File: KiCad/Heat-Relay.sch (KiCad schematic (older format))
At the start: 6 parts

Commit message: controller board schematic complete
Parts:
- gave numbers to parts that had none: 6
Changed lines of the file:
@@
 $Descr A4 11693 8268
 encoding utf-8
-Sheet 3 5
+Sheet 3 6
 Title ""
 Date ""
@@
 Heat
 $Comp
-L G5LE-1A-E_DC12 K?
+L G5LE-1A-E_DC12 K1
 U 1 1 568008CE
 P 7100 3250
-F 0 "K?" H 7850 3350 50  0000 L CNN
+F 0 "K1" H 7850 3350 50  0000 L CNN
 F 1 "G5LE-1A-E_DC12" H 7850 3200 50  0000 L CNN
 F 2 "" H 7100 3250 50  0000 C CNN
@@
 $EndComp
 $Comp
-L MJE340 Q?
+L MJE340 Q2
 U 1 1 5680095F
 P 6300 4400
-F 0 "Q?" H 6500 4475 50  0000 L CNN
+F 0 "Q2" H 6500 4475 50  0000 L CNN
 F 1 "MJE340" H 6500 4400 50  0000 L CNN
 F 2 "TO-126" H 6500 4325 50  0000 L CIN
@@
 $EndComp
 $Comp
-L D D?
+L D D1
 U 1 1 56800A86
 P 6400 3250
-F 0 "D?" V 6300 3100 50  0000 R CNN
+F 0 "D1" V 6300 3100 50  0000 R CNN
 F 1 "V*A(max) > 0.4 W" V 6450 3100 50  0000 R CNN
 F 2 "" H 6400 3250 50  0000 C CNN
@@
 HeatLive
 $Comp
-L VAA #PWR?
+L VAA #PWR28
 U 1 1 56800D0A
 P 7650 2200
-F 0 "#PWR?" H 7650 2050 50  0001 C CNN
+F 0 "#PWR28" H 7650 2050 50  0001 C CNN
 F 1 "VAA" H 7650 2350 50  0000 C CNN
 F 2 "" H 7650 2200 50  0000 C CNN
@@
 $EndComp
 $Comp
-L +12V #PWR?
+L +12V #PWR26
 U 1 1 56800DC1
 P 6400 2200
-F 0 "#PWR?" H 6400 2050 50  0001 C CNN
+F 0 "#PWR26" H 6400 2050 50  0001 C CNN
 F 1 "+12V" H 6400 2340 50  0000 C CNN
 F 2 "" H 6400 2200 50  0000 C CNN
@@
 DoorC2
 $Comp
-L R R?
+L R R23
 U 1 1 56800FE2
 P 5500 4950
-F 0 "R?" V 5580 4950 50  0000 C CNN
+F 0 "R23" V 5580 4950 50  0000 C CNN
 F 1 "333" V 5500 4950 50  0000 C CNN
 F 2 "" V 5430 4950 50  0000 C CNN
@@
 $EndComp
 $Comp
-L R R?
+L R R22
 U 1 1 5680103F
 P 3550 4400
-F 0 "R?" V 3630 4400 50  0000 C CNN
+F 0 "R22" V 3630 4400 50  0000 C CNN
 F 1 "1k" V 3550 4400 50  0000 C CNN
 F 2 "" V 3480 4400 50  0000 C CNN
@@
 $EndComp
 $Comp
-L R R?
+L R R21
 U 1 1 5680107F
 P 3000 3950
-F 0 "R?" V 3080 3950 50  0000 C CNN
+F 0 "R21" V 3080 3950 50  0000 C CNN
 F 1 "10k" V 3000 3950 50  0000 C CNN
 F 2 "" V 2930 3950 50  0000 C CNN
@@
 $EndComp
 $Comp
-L VDD #PWR?
+L VDD #PWR24
 U 1 1 56801231
 P 3000 3300
-F 0 "#PWR?" H 3000 3150 50  0001 C CNN
+F 0 "#PWR24" H 3000 3150 50  0001 C CNN
 F 1 "VDD" H 3000 3450 50  0000 C CNN
 F 2 "" H 3000 3300 50  0000 C CNN
@@
 Connection ~ 5500 4400
 $Comp
-L GND #PWR?
+L GND #PWR25
 U 1 1 56801366
 P 5500 5400
-F 0 "#PWR?" H 5500 5150 50  0001 C CNN
+F 0 "#PWR25" H 5500 5150 50  0001 C CNN
 F 1 "GND" H 5500 5250 50  0000 C CNN
 F 2 "" H 5500 5400 50  0000 C CNN
@@
 $EndComp
 $Comp
-L GND #PWR?
+L GND #PWR27
 U 1 1 56801386
 P 6400 5400
-F 0 "#PWR?" H 6400 5150 50  0001 C CNN
+F 0 "#PWR27" H 6400 5150 50  0001 C CNN
 F 1 "GND" H 6400 5250 50  0000 C CNN
 F 2 "" H 6400 5400 50  0000 C CNN

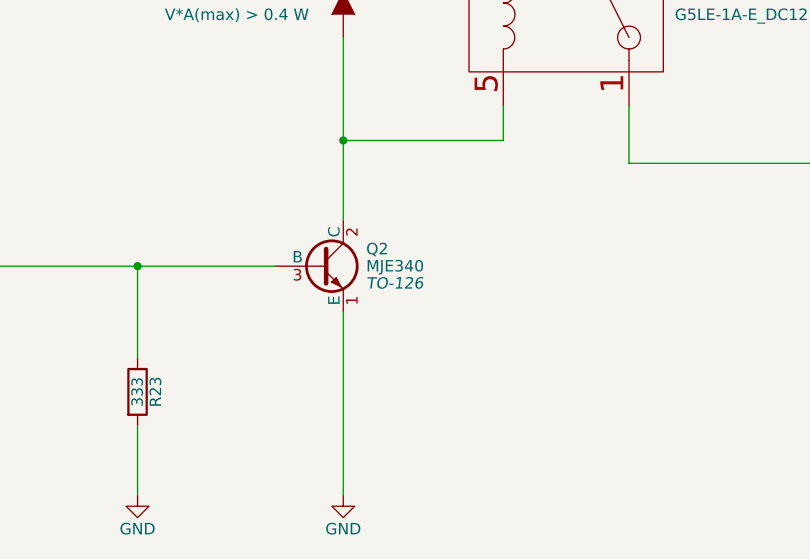
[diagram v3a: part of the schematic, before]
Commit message: HeatOn fix, replaced R1-8 with array
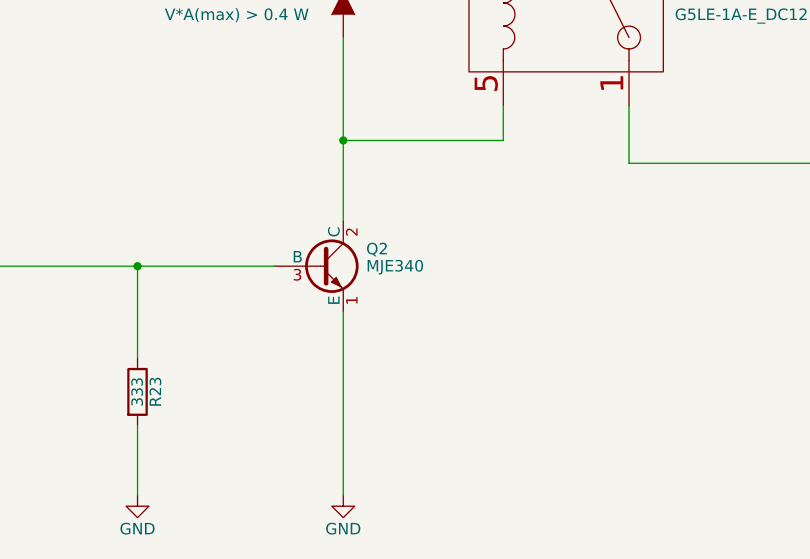
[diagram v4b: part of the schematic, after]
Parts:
- Q2: footprint TO-126 -> (none)
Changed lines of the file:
@@
 F 0 "K1" H 7850 3350 50  0000 L CNN
 F 1 "G5LE-1A-E_DC12" H 7850 3200 50  0000 L CNN
-F 2 "" H 7100 3250 50  0000 C CNN
+F 2 "" H 7100 3250 50  0001 C CNN
 F 3 "" H 7100 3250 50  0000 C CNN
 	1    7100 3250
@@
 F 0 "Q2" H 6500 4475 50  0000 L CNN
 F 1 "MJE340" H 6500 4400 50  0000 L CNN
-F 2 "TO-126" H 6500 4325 50  0000 L CIN
+F 2 "" H 6500 4325 50  0001 L CIN
 F 3 "" H 6300 4400 50  0000 L CNN
 	1    6300 4400
@@
 F 0 "D1" V 6300 3100 50  0000 R CNN
 F 1 "V*A(max) > 0.4 W" V 6450 3100 50  0000 R CNN
-F 2 "" H 6400 3250 50  0000 C CNN
+F 2 "" H 6400 3250 50  0001 C CNN
 F 3 "" H 6400 3250 50  0000 C CNN
 	1    6400 3250
@@
 HeatLive
 $Comp
-L VAA #PWR28
+L VAA #PWR024
 U 1 1 56800D0A
 P 7650 2200
-F 0 "#PWR28" H 7650 2050 50  0001 C CNN
+F 0 "#PWR024" H 7650 2050 50  0001 C CNN
 F 1 "VAA" H 7650 2350 50  0000 C CNN
 F 2 "" H 7650 2200 50  0000 C CNN
@@
 $EndComp
 $Comp
-L +12V #PWR26
+L +12V #PWR025
 U 1 1 56800DC1
 P 6400 2200
-F 0 "#PWR26" H 6400 2050 50  0001 C CNN
+F 0 "#PWR025" H 6400 2050 50  0001 C CNN
 F 1 "+12V" H 6400 2340 50  0000 C CNN
 F 2 "" H 6400 2200 50  0000 C CNN
@@
 F 0 "R23" V 5580 4950 50  0000 C CNN
 F 1 "333" V 5500 4950 50  0000 C CNN
-F 2 "" V 5430 4950 50  0000 C CNN
+F 2 "" V 5430 4950 50  0001 C CNN
 F 3 "" H 5500 4950 50  0000 C CNN
 	1    5500 4950
@@
 F 0 "R22" V 3630 4400 50  0000 C CNN
 F 1 "1k" V 3550 4400 50  0000 C CNN
-F 2 "" V 3480 4400 50  0000 C CNN
+F 2 "" V 3480 4400 50  0001 C CNN
 F 3 "" H 3550 4400 50  0000 C CNN
 	1    3550 4400
@@
 F 0 "R21" V 3080 3950 50  0000 C CNN
 F 1 "10k" V 3000 3950 50  0000 C CNN
-F 2 "" V 2930 3950 50  0000 C CNN
+F 2 "" V 2930 3950 50  0001 C CNN
 F 3 "" H 3000 3950 50  0000 C CNN
 	1    3000 3950
@@
 $EndComp
 $Comp
-L VDD #PWR24
+L VDD #PWR026
 U 1 1 56801231
 P 3000 3300
-F 0 "#PWR24" H 3000 3150 50  0001 C CNN
+F 0 "#PWR026" H 3000 3150 50  0001 C CNN
 F 1 "VDD" H 3000 3450 50  0000 C CNN
 F 2 "" H 3000 3300 50  0000 C CNN
@@
 Connection ~ 5500 4400
 $Comp
-L GND #PWR25
+L GND #PWR027
 U 1 1 56801366
 P 5500 5400
-F 0 "#PWR25" H 5500 5150 50  0001 C CNN
+F 0 "#PWR027" H 5500 5150 50  0001 C CNN
 F 1 "GND" H 5500 5250 50  0000 C CNN
 F 2 "" H 5500 5400 50  0000 C CNN
@@
 $EndComp
 $Comp
-L GND #PWR27
+L GND #PWR028
 U 1 1 56801386
 P 6400 5400
-F 0 "#PWR27" H 6400 5150 50  0001 C CNN
+F 0 "#PWR028" H 6400 5150 50  0001 C CNN
 F 1 "GND" H 6400 5250 50  0000 C CNN
 F 2 "" H 6400 5400 50  0000 C CNN

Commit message: kicad resistor package associations complete
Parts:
- R21, R22, R23: footprint (none) -> Resistors_ThroughHole:Resistor_Horizontal_RM10mm
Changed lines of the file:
@@
 F 0 "R23" V 5580 4950 50  0000 C CNN
 F 1 "333" V 5500 4950 50  0000 C CNN
-F 2 "" V 5430 4950 50  0001 C CNN
+F 2 "Resistors_ThroughHole:Resistor_Horizontal_RM10mm" V 5430 4950 50  0001 C CNN
 F 3 "" H 5500 4950 50  0000 C CNN
 	1    5500 4950
@@
 F 0 "R22" V 3630 4400 50  0000 C CNN
 F 1 "1k" V 3550 4400 50  0000 C CNN
-F 2 "" V 3480 4400 50  0001 C CNN
+F 2 "Resistors_ThroughHole:Resistor_Horizontal_RM10mm" V 3480 4400 50  0001 C CNN
 F 3 "" H 3550 4400 50  0000 C CNN
 	1    3550 4400
@@
 F 0 "R21" V 3080 3950 50  0000 C CNN
 F 1 "10k" V 3000 3950 50  0000 C CNN
-F 2 "" V 2930 3950 50  0001 C CNN
+F 2 "Resistors_ThroughHole:Resistor_Horizontal_RM10mm" V 2930 3950 50  0001 C CNN
 F 3 "" H 3000 3950 50  0000 C CNN
 	1    3000 3950

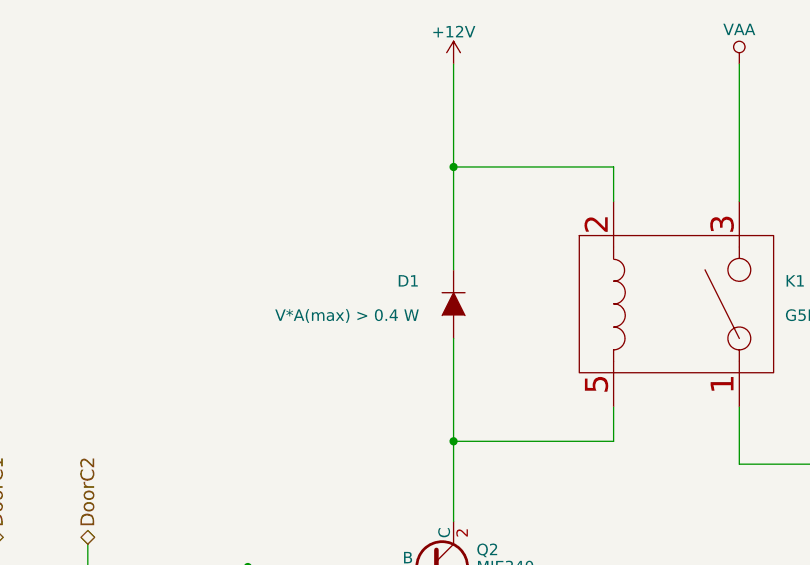
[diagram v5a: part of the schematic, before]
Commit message: capacitors and diode part associations
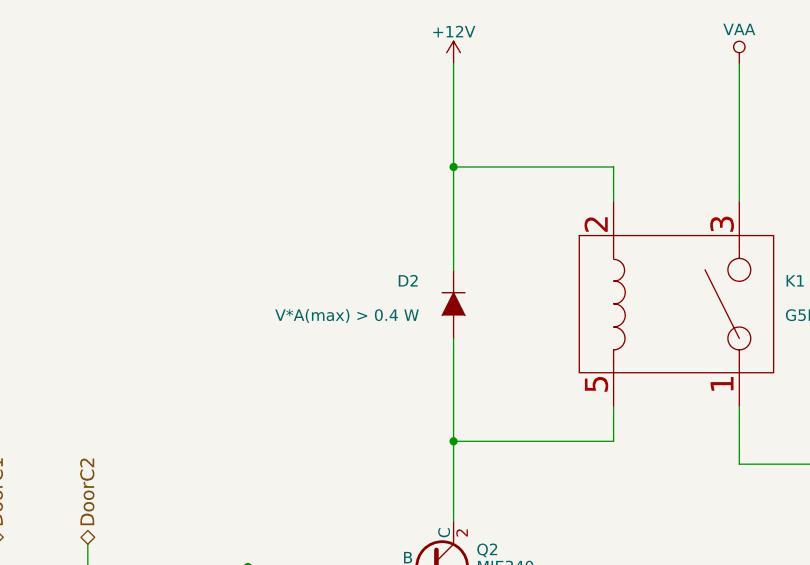
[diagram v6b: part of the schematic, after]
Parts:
- D2: renamed from D1; footprint (none) -> Discret:D3
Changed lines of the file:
@@
 $EndComp
 $Comp
-L D D1
+L D D2
 U 1 1 56800A86
 P 6400 3250
-F 0 "D1" V 6300 3100 50  0000 R CNN
+F 0 "D2" V 6300 3100 50  0000 R CNN
 F 1 "V*A(max) > 0.4 W" V 6450 3100 50  0000 R CNN
-F 2 "" H 6400 3250 50  0001 C CNN
+F 2 "Discret:D3" H 6400 3250 50  0001 C CNN
 F 3 "" H 6400 3250 50  0000 C CNN
 	1    6400 3250

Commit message: footprint associations complete
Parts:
- K1: footprint (none) -> Easy-PCB-footprints:G5LE-1A-E_DC12
- Q2: footprint (none) -> Easy-PCB-footprints:MJE3x0
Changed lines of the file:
@@
 F 0 "K1" H 7850 3350 50  0000 L CNN
 F 1 "G5LE-1A-E_DC12" H 7850 3200 50  0000 L CNN
-F 2 "" H 7100 3250 50  0001 C CNN
+F 2 "Easy-PCB-footprints:G5LE-1A-E_DC12" H 7100 3250 50  0001 C CNN
 F 3 "" H 7100 3250 50  0000 C CNN
 	1    7100 3250
@@
 F 0 "Q2" H 6500 4475 50  0000 L CNN
 F 1 "MJE340" H 6500 4400 50  0000 L CNN
-F 2 "" H 6500 4325 50  0001 L CIN
+F 2 "Easy-PCB-footprints:MJE3x0" H 6500 4325 50  0001 L CIN
 F 3 "" H 6300 4400 50  0000 L CNN
 	1    6300 4400

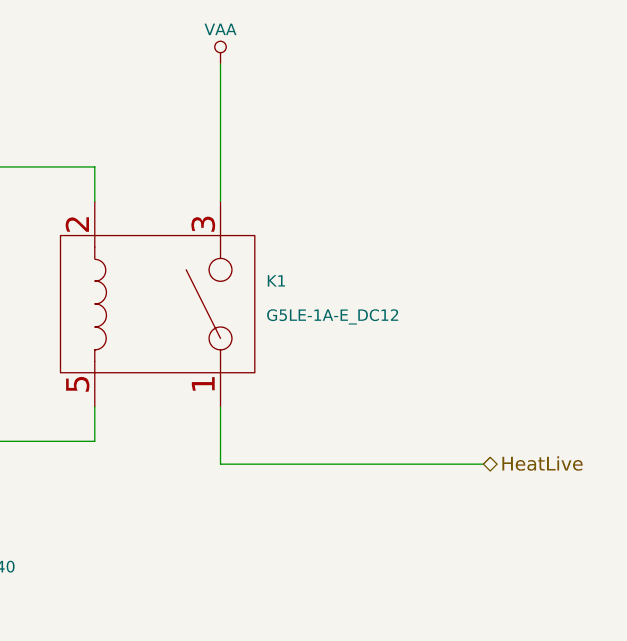
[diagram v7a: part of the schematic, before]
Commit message: power port, switch, transformer, and relay in place
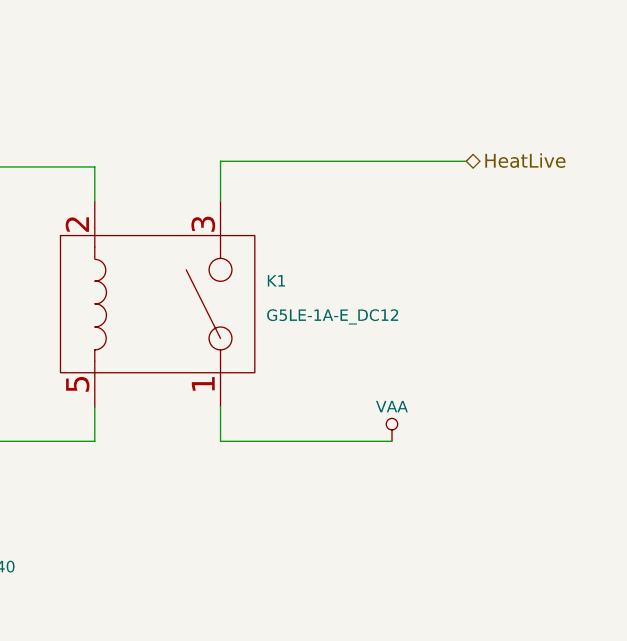
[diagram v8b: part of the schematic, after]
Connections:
- net HeatLive: now also K1.3 (contact_2); no longer K1.1 (contact_1)
- net VAA: now also K1.1 (contact_1); no longer K1.3 (contact_2)
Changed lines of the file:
@@
 	0    1    1    0
 $EndComp
-Text HLabel 8800 3950 2    60   BiDi ~ 0
+Text HLabel 8725 2625 2    60   BiDi ~ 0
 HeatLive
 $Comp
 L VAA #PWR024
 U 1 1 56800D0A
-P 7650 2200
-F 0 "#PWR024" H 7650 2050 50  0001 C CNN
-F 1 "VAA" H 7650 2350 50  0000 C CNN
-F 2 "" H 7650 2200 50  0000 C CNN
-F 3 "" H 7650 2200 50  0000 C CNN
-	1    7650 2200
+P 8400 3850
+F 0 "#PWR024" H 8400 3700 50  0001 C CNN
+F 1 "VAA" H 8400 4000 50  0000 C CNN
+F 2 "" H 8400 3850 50  0000 C CNN
+F 3 "" H 8400 3850 50  0000 C CNN
+	1    8400 3850
 	1    0    0    -1
 $EndComp
@@
 	1    0    0    -1
 $EndComp
-Wire Wire Line
-	7650 2200 7650 2800
-Wire Wire Line
-	8800 3950 7650 3950
-Wire Wire Line
-	7650 3950 7650 3700
-Wire Wire Line
-	6400 2200 6400 3100
-Wire Wire Line
-	6400 2650 7100 2650
-Wire Wire Line
-	7100 2650 7100 2800
-Connection ~ 6400 2650
-Wire Wire Line
-	6400 3400 6400 4200
-Wire Wire Line
-	7100 3700 7100 3850
-Wire Wire Line
-	7100 3850 6400 3850
-Connection ~ 6400 3850
 Text HLabel 4400 4300 1    60   BiDi ~ 0
 DoorC1
@@
 	1    0    0    -1
 $EndComp
-Wire Wire Line
-	3000 3300 3000 3800
-Wire Wire Line
-	2400 4400 3400 4400
-Wire Wire Line
-	3000 4100 3000 4400
-Connection ~ 3000 4400
-Wire Wire Line
-	3700 4400 4400 4400
-Wire Wire Line
-	4400 4400 4400 4300
-Wire Wire Line
-	4800 4300 4800 4400
-Wire Wire Line
-	4800 4400 6100 4400
-Wire Wire Line
-	5500 4800 5500 4400
-Connection ~ 5500 4400
 $Comp
 L GND #PWR027
@@
 $EndComp
 Wire Wire Line
+	6400 2200 6400 3100
+Wire Wire Line
+	6400 2650 7100 2650
+Wire Wire Line
+	7100 2650 7100 2800
+Connection ~ 6400 2650
+Wire Wire Line
+	6400 3400 6400 4200
+Wire Wire Line
+	7100 3700 7100 3850
+Wire Wire Line
+	7100 3850 6400 3850
+Connection ~ 6400 3850
+Wire Wire Line
+	3000 3300 3000 3800
+Wire Wire Line
+	2400 4400 3400 4400
+Wire Wire Line
+	3000 4100 3000 4400
+Connection ~ 3000 4400
+Wire Wire Line
+	3700 4400 4400 4400
+Wire Wire Line
+	4400 4400 4400 4300
+Wire Wire Line
+	4800 4300 4800 4400
+Wire Wire Line
+	4800 4400 6100 4400
+Wire Wire Line
+	5500 4800 5500 4400
+Connection ~ 5500 4400
+Wire Wire Line
 	5500 5100 5500 5400
 Wire Wire Line
 	6400 4600 6400 5400
+Wire Wire Line
+	8725 2625 7650 2625
+Wire Wire Line
+	7650 2625 7650 2800
+Wire Wire Line
+	7650 3700 7650 3850
+Wire Wire Line
+	7650 3850 8400 3850
 $EndSCHEMATC
